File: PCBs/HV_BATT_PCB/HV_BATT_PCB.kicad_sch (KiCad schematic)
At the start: 66 parts, among them J47 Conn_01x02_Male, J48 Conn_01x10_Male, J49 Conn_01x08_Male, J50 Conn_01x02_Male, J51 Conn_01x02_Male, J52 Conn_01x02_Male, J53 Conn_01x02_Male, J54 Conn_01x14_Male, J55 Conn_01x06_Male, J56 Conn_01x04_Male, K10 LV_BATT_FAN, K7 PUMP, K8 FAN_R, K9 FAN_L, Q18 IRF640, Q19 IRF640, Q20 IRF640, U27 LR8, U28 LR8, U29 LR8, U30 LR8, U31 LR8, U32 LM311, U33 LR8, U34 4N35, U35 NE555P

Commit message: update schematics snapshot
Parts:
- removed C10: 1uF, Capacitor_THT:C_Disc_D4.3mm_W1.9mm_P5.00mm, symbol Device:C_Small
- removed C11: 1uF, Capacitor_THT:C_Axial_L3.8mm_D2.6mm_P15.00mm_Horizontal, symbol Device:C
- removed C12: 1uF, Capacitor_THT:CP_Radial_D8.0mm_P5.00mm, symbol Device:C_Polarized
- removed C7, C8: 2.2uF, Capacitor_THT:CP_Radial_D8.0mm_P5.00mm, symbol Device:C
- removed C9: 1nF, Capacitor_THT:C_Disc_D4.3mm_W1.9mm_P5.00mm, symbol Device:C_Small
- removed D28, D29, D31, D32, D33, D34: 1N5349, Diode_THT:D_DO-15_P10.16mm_Horizontal, symbol Diode:1N53xxB
- removed D30: TVS, Diode_SMD:D_SMC, symbol Diode:1.5KExxA
- removed F4: 3A Fuse, footprint:Fuse_Holder(GF-205B), symbol Device:Fuse
- removed J47: Conn_01x02_Male, Connector_AMASS:AMASS_XT30U-F_1x02_P5.0mm_Vertical, symbol Connector:Conn_01x02_Male
- removed J48: Conn_01x10_Male, Connector_Molex:Molex_Micro-Fit_3.0_43650-1015_1x10_P3.00mm_Vertical, symbol Connector:Conn_01x10_Male
- removed J49: Conn_01x08_Male, Connector_PinHeader_2.54mm:PinHeader_1x08_P2.54mm_Vertical, symbol Connector:Conn_01x08_Male
- removed J50: Conn_01x02_Male, Connector_PinHeader_2.54mm:PinHeader_2x01_P2.54mm_Vertical, symbol 11:Conn_01x02_Male
- removed J51, J52: Conn_01x02_Male, Connector_Molex:Molex_Micro-Fit_3.0_43650-0215_1x02_P3.00mm_Vertical, symbol Connector:Conn_01x02_Male
- removed J53: Conn_01x02_Male, Connector_PinHeader_2.54mm:PinHeader_2x01_P2.54mm_Vertical, symbol Connector:Conn_01x02_Male
- removed J54: Conn_01x14_Male, Connector_PinHeader_2.54mm:PinHeader_1x14_P2.54mm_Vertical, symbol Connector:Conn_01x14_Male
- removed J55: Conn_01x06_Male, Connector_PinHeader_2.54mm:PinHeader_1x06_P2.54mm_Vertical, symbol Connector:Conn_01x06_Male
- removed J56: Conn_01x04_Male, Connector_PinHeader_2.54mm:PinHeader_1x04_P2.54mm_Vertical, symbol Connector:Conn_01x04_Male
- removed K10: LV_BATT_FAN, Goolgle_Drive_Library:HR702, symbol Relay:DIPxx-1Cxx-51x
- removed K7: PUMP, Goolgle_Drive_Library:HR702, symbol Relay:DIPxx-1Cxx-51x
- removed K8: FAN_R, Goolgle_Drive_Library:HR702, symbol Relay:DIPxx-1Cxx-51x
- removed K9: FAN_L, Goolgle_Drive_Library:HR702, symbol Relay:DIPxx-1Cxx-51x
- removed Q18, Q19, Q20: IRF640, Goolgle_Drive_Library:IRF640NPBF, symbol Device:Q_NMOS_GDS
- removed R57, R58, R59, R60, R62, R63, R65, R67: 4.7M, Resistor_THT:R_Axial_DIN0207_L6.3mm_D2.5mm_P10.16mm_Horizontal, symbol Device:R_US
- removed R61: 1M, Resistor_THT:R_Axial_DIN0207_L6.3mm_D2.5mm_P10.16mm_Horizontal, symbol Device:R_US
- removed R64: 390k, Resistor_THT:R_Axial_DIN0207_L6.3mm_D2.5mm_P10.16mm_Horizontal, symbol Device:R_US
- removed R66: 4.7k, Resistor_THT:R_Axial_DIN0207_L6.3mm_D2.5mm_P10.16mm_Horizontal, symbol Device:R_US
- removed R68: 18k, Resistor_THT:R_Axial_DIN0207_L6.3mm_D2.5mm_P10.16mm_Horizontal, symbol Device:R_US
- removed R69: 12k, Resistor_THT:R_Axial_DIN0207_L6.3mm_D2.5mm_P10.16mm_Horizontal, symbol Device:R_US
- removed R70, R74: 10k, Resistor_THT:R_Axial_DIN0207_L6.3mm_D2.5mm_P10.16mm_Horizontal, symbol Device:R_US
- removed R71, R75: 2k2, Resistor_THT:R_Axial_DIN0207_L6.3mm_D2.5mm_P10.16mm_Horizontal, symbol Device:R_US
- removed R72: 1k, Resistor_THT:R_Axial_DIN0207_L6.3mm_D2.5mm_P10.16mm_Horizontal, symbol Device:R_US
- removed R73: 100k, Resistor_THT:R_Axial_DIN0207_L6.3mm_D2.5mm_P10.16mm_Horizontal, symbol Device:R_US
- removed R76, R77: 240k, Resistor_THT:R_Axial_DIN0207_L6.3mm_D2.5mm_P10.16mm_Horizontal, symbol Device:R_US
- removed U27, U28, U29, U30, U31, U33: LR8, Goolgle_Drive_Library:LR8N3-G, symbol Regulator_Linear:LR8K4-G
- removed U32: LM311, Goolgle_Drive_Library:LM311P, symbol Comparator:LM311
- removed U34: 4N35, Goolgle_Drive_Library:4N35, symbol Isolator:4N35
- removed U35: NE555P, Goolgle_Drive_Library:NE555P, symbol Timer:NE555P
- added BMS1: Conn_01x08_Male, Connector_PinHeader_2.54mm:PinHeader_1x08_P2.54mm_Vertical, symbol Connector:Conn_01x08_Male
- added C1, C2: 2.2uF, Capacitor_THT:CP_Radial_D8.0mm_P5.00mm, symbol Device:C
- added C3: 1nF, Capacitor_THT:C_Disc_D4.3mm_W1.9mm_P5.00mm, symbol Device:C_Small
- added C4: 1uF, Capacitor_THT:C_Disc_D4.3mm_W1.9mm_P5.00mm, symbol Device:C_Small
- added C5: 1uF, Capacitor_THT:C_Axial_L3.8mm_D2.6mm_P15.00mm_Horizontal, symbol Device:C
- added C6: 1uF, Capacitor_THT:CP_Radial_D8.0mm_P5.00mm, symbol Device:C_Polarized
- added D1, D2, D4, D5, D6, D7: 1N5349, Diode_THT:D_DO-15_P10.16mm_Horizontal, symbol Diode:1N53xxB
- added D3: TVS, Diode_SMD:D_SMC, symbol Diode:1.5KExxA
- added F1: SMCJ440A, Fuse:Fuseholder_Cylinder-5x20mm_Schurter_0031_8201_Horizontal_Open, symbol Device:Fuse
- added FAN,GND_{AIR1: Conn_01x04_Male, Connector_PinHeader_2.54mm:PinHeader_1x04_P2.54mm_Vertical, symbol Connector:Conn_01x04_Male
- added HV_{PCB1, J1, PRECHARGE2: Conn_01x02_Male, Connector_Molex:Molex_Micro-Fit_3.0_43650-0215_1x02_P3.00mm_Vertical, symbol Connector:Conn_01x02_Male
- added IMD1: Conn_01x06_Male, Connector_PinHeader_2.54mm:PinHeader_1x06_P2.54mm_Vertical, symbol Connector:Conn_01x06_Male
- added K1: PUMP, Goolgle_Drive_Library:HR702, symbol Relay:DIPxx-1Cxx-51x
- added K2: FAN_R, Goolgle_Drive_Library:HR702, symbol Relay:DIPxx-1Cxx-51x
- added K3: FAN_L, Goolgle_Drive_Library:HR702, symbol Relay:DIPxx-1Cxx-51x
- added K4: LV_BATT_FAN, Goolgle_Drive_Library:HR702, symbol Relay:DIPxx-1Cxx-51x
- added Q1, Q2, Q3: IRF640, Goolgle_Drive_Library:IRF640NPBF, symbol Device:Q_NMOS_GDS
- added R1, R11, R2, R3, R4, R6, R7, R9: 4.7M, Resistor_THT:R_Axial_DIN0207_L6.3mm_D2.5mm_P10.16mm_Horizontal, symbol Device:R_US
- added R10: 4.7k, Resistor_THT:R_Axial_DIN0207_L6.3mm_D2.5mm_P10.16mm_Horizontal, symbol Device:R_US
- added R12: 18k, Resistor_THT:R_Axial_DIN0207_L6.3mm_D2.5mm_P10.16mm_Horizontal, symbol Device:R_US
- added R13: 12k, Resistor_THT:R_Axial_DIN0207_L6.3mm_D2.5mm_P10.16mm_Horizontal, symbol Device:R_US
- added R14, R18: 10k, Resistor_THT:R_Axial_DIN0207_L6.3mm_D2.5mm_P10.16mm_Horizontal, symbol Device:R_US
- added R15, R19: 2k2, Resistor_THT:R_Axial_DIN0207_L6.3mm_D2.5mm_P10.16mm_Horizontal, symbol Device:R_US
- added R16: 1k, Resistor_THT:R_Axial_DIN0207_L6.3mm_D2.5mm_P10.16mm_Horizontal, symbol Device:R_US
- added R17: 100k, Resistor_THT:R_Axial_DIN0207_L6.3mm_D2.5mm_P10.16mm_Horizontal, symbol Device:R_US
- added R20, R21: 240k, Resistor_THT:R_Axial_DIN0207_L6.3mm_D2.5mm_P10.16mm_Horizontal, symbol Device:R_US
- added R5: 1M, Resistor_THT:R_Axial_DIN0207_L6.3mm_D2.5mm_P10.16mm_Horizontal, symbol Device:R_US
- added R8: 390k, Resistor_THT:R_Axial_DIN0207_L6.3mm_D2.5mm_P10.16mm_Horizontal, symbol Device:R_US
- added TEMP1: Conn_01x02_Male, Connector_PinHeader_2.54mm:PinHeader_2x01_P2.54mm_Vertical, symbol 11:Conn_01x02_Male
- added U1, U2, U3, U4, U5, U7: LR8, Goolgle_Drive_Library:LR8N3-G, symbol Regulator_Linear:LR8K4-G
- added U6: LM311, Goolgle_Drive_Library:LM311P, symbol Comparator:LM311
- added U8: 4N35, Goolgle_Drive_Library:4N35, symbol Isolator:4N35
- added U9: NE555P, Goolgle_Drive_Library:NE555P, symbol Timer:NE555P
- added VI1: Conn_01x02_Male, Connector_PinHeader_2.54mm:PinHeader_2x01_P2.54mm_Vertical, symbol Connector:Conn_01x02_Male
- added asdf1: Conn_01x10_Male, Connector_Molex:Molex_Micro-Fit_3.0_43650-1015_1x10_P3.00mm_Vertical, symbol Connector:Conn_01x10_Male
- added dff1: Conn_01x14_Male, Connector_PinHeader_2.54mm:PinHeader_1x14_P2.54mm_Vertical, symbol Connector:Conn_01x14_Male
- F2: value SMCJ440A -> 1A Fuse; footprint Goolgle_Drive_Library:Fuse_Holder(GF-205B) -> Fuse:Fuseholder_Cylinder-5x20mm_Schurter_0031_8201_Horizontal_Open
- F3: value 1A Fuse -> 3A Fuse; footprint footprint:Fuse_Holder(GF-205B) -> Fuse:Fuseholder_Cylinder-5x20mm_Schurter_0031_8201_Horizontal_Open
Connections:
- net GND is gone; now on net GND_AIR: PRECHARGE1.5 (COIL_2)
- net BMS_FAULT: now also BMS1.2 (Pin_2), dff1.4 (Pin_4)
- net CAN_H_{BMS: now also BMS1.4 (Pin_4), dff1.8 (Pin_8)
- net CAN_L_{BMS: now also BMS1.5 (Pin_5), dff1.9 (Pin_9)
- net CHARGER_SAFETY: now also BMS1.7 (Pin_7), dff1.12 (Pin_12)
- net CHARGE_POWER: now also BMS1.6 (Pin_6), dff1.11 (Pin_11)
- net GND_AIR: now also BMS1.3 (Pin_3), FAN,GND_{AIR1.3 (Pin_3), IMD1.1 (Pin_1), IMD1.3 (Pin_3), IMD1.4 (Pin_4), Q1.3 (S), Q2.3 (S), Q3.3 (S), R17.1, R19.2, TEMP1.2 (Pin_2), dff1.2 (Pin_2)
- net HV_{PCB}+: now also D1.1 (K), HV_{PCB1.1 (Pin_1), R1.1
- net HV_{PCB}-: now also C1.2, C2.2, C5.2, D7.2 (A), HV_{PCB1.2 (Pin_2), R11.2, R12.2, R16.2, R5.2, R8.2, U6.1 (GND), U6.4 (V-), U8.2
- net IMD_FAULT: now also IMD1.5 (Pin_5), R19.1, dff1.3 (Pin_3)
- net LV_{BATT_FAN}+: now also FAN,GND_{AIR1.1 (Pin_1), K2.14
- net LV_{BATT_FAN}-: now also FAN,GND_{AIR1.2 (Pin_2), asdf1.7 (Pin_7), asdf1.8 (Pin_8), asdf1.9 (Pin_9)
- net LV_{BMS}+: now also F2.2, BMS1.1 (Pin_1); no longer F3.2
- net LV_{COOLING1}: now also K1.7, K1.8, K2.7, K2.8, K3.7, K3.8, K4.7, K4.8
- net LV_{FAN_L}+: now also K3.14, asdf1.5 (Pin_5)
- net LV_{FAN_R}+: now also K4.14, asdf1.4 (Pin_4)
- net LV_{IMD}+: now also F3.2, IMD1.2 (Pin_2)
- net LV_{PACK}+: now also F2.1, K1.2, K2.2, K3.2, K4.2, R18.1, R20.2, TEMP1.1 (Pin_1), U8.5, U9.4 (R), U9.8 (VCC), asdf1.3 (Pin_3), dff1.1 (Pin_1)
- net LV_{PUMP}+: now also K1.14, asdf1.6 (Pin_6)
- net ON_{BATT_FAN}: now also K2.6, dff1.7 (Pin_7)
- net ON_{COOLING: now also dff1.13 (Pin_13)
- net ON_{PUMP}: now also K1.6, dff1.5 (Pin_5)
- net ON_{RAD_FAN}: now also K3.6, K4.6, dff1.6 (Pin_6)
- net PRECHARGE_DRIVE: now also dff1.10 (Pin_10)
- net RELAY_PRECHARGE: now also PRECHARGE2.1 (Pin_1)
- net R_PRECHARGE: now also PRECHARGE2.2 (Pin_2)
- net TSAL_GREEN: now also Q1.2 (D), asdf1.1 (Pin_1)
- net TSAL_RED: now also U9.3 (Q), asdf1.2 (Pin_2)
- net VI_LED+: now also C5.1, R13.1, U4.2 (OUT), U5.2 (OUT), U7.2 (OUT), VI1.1 (Pin_1)
- net VI_LED-: now also R16.1, VI1.2 (Pin_2)
- net at PS2.1 (+VIN): now also D3.1 (A1), F1.2; no longer F2.2
- net at PS2.3 (-VIN): now also D3.2 (A2), J1.1 (Pin_1)
- net at PS1.6 (+VOUT): now also C4.1, R14.1, R6.1, U6.8 (V+)
- new net: R14.2, R15.1, U6.7
- new net: R15.2, U8.1
- new net: R6.2, R7.1
- new net: C6.2, Q3.2 (D), U9.1 (GND)
- new net: C6.1, R21.1, U9.2 (TR), U9.6 (THR)
- new net: R20.1, R21.2, U9.7 (DIS)
- new net: C1.1, D6.2 (A), U1.1 (IN), U2.1 (IN), U3.1 (IN)
- new net: C2.1, R10.1, U1.2 (OUT), U2.2 (OUT), U3.2 (OUT), U4.1 (IN), U5.1 (IN), U7.1 (IN)
- new net: R10.2, R8.1, U1.3 (ADJ), U2.3 (ADJ), U3.3 (ADJ)
- new net: D5.2 (A), D6.1 (K)
- new net: R2.2, R3.1
- new net: R3.2, R4.1
- new net: F1.1, J1.2 (Pin_2)
- new net: Q2.1 (G), Q3.1 (G), R17.2, U8.4
- new net: C3.1, R11.1, R9.2, U6.3 (-)
- new net: D2.2 (A), D4.1 (K)
- new net: D4.2 (A), D5.1 (K)
- new net: R12.1, R13.2, U4.3 (ADJ), U5.3 (ADJ), U7.3 (ADJ)
- new net: D1.2 (A), D2.1 (K)
- new net: Q1.1 (G), Q2.2 (D), R18.2
- new net: C3.2, D7.1 (K), R4.2, R5.1, U6.2 (+)
- new net: R1.2, R2.1
- new net: C4.2, U6.5 (BAL), U6.6 (STRB)
- new net: R7.2, R9.1
- no-connect marks 17 -> 22
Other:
- note added: "LV, HV distance..."

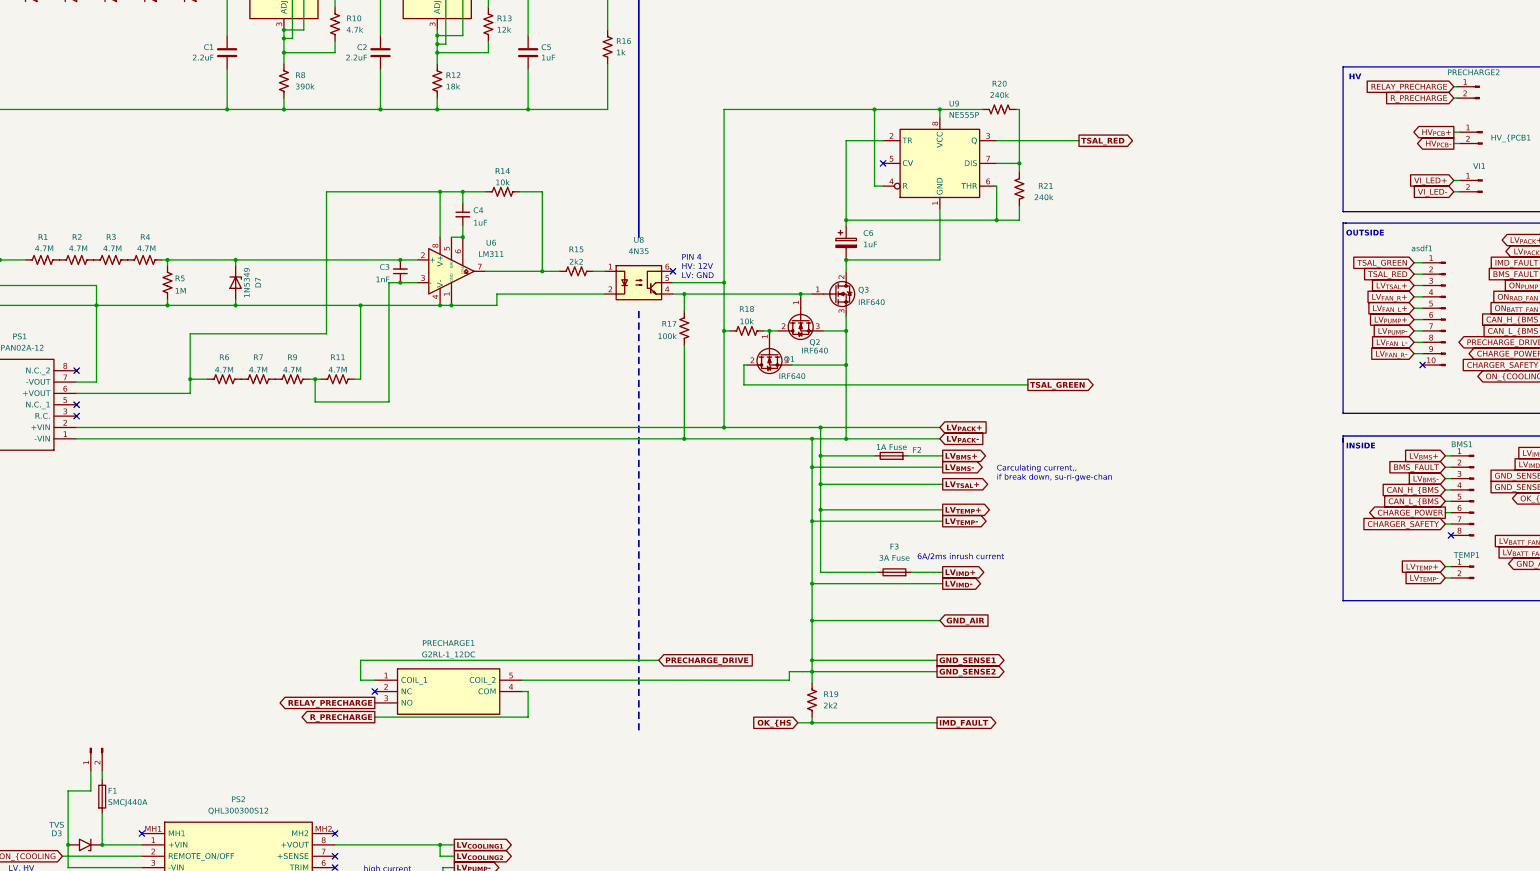
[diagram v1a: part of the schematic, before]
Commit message: update: schematics and wirings to current state
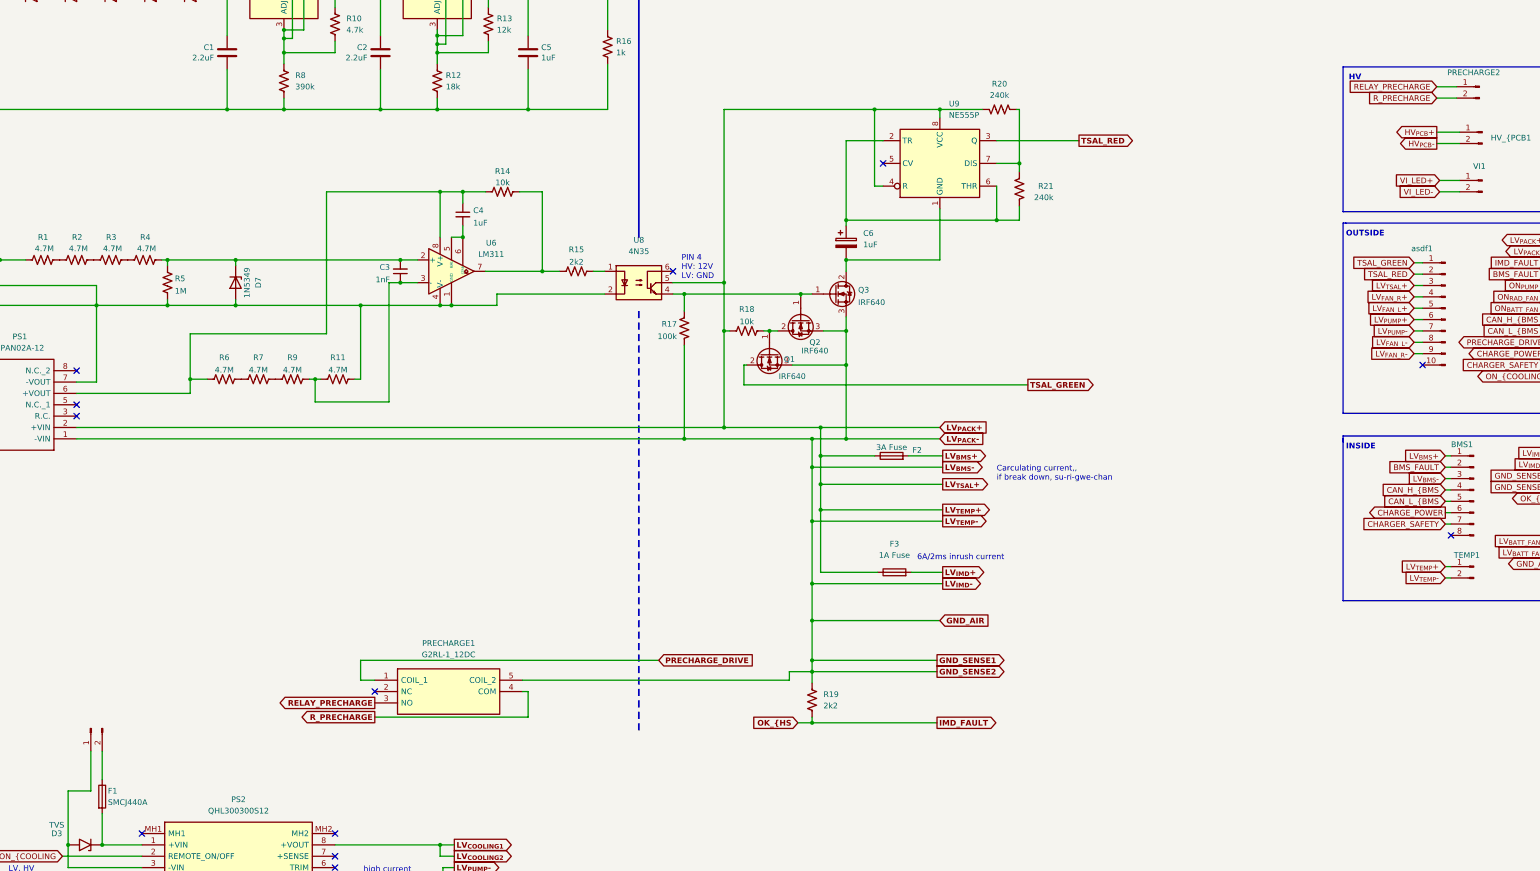
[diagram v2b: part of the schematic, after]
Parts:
- F2: value 1A Fuse -> 3A Fuse
- F3: value 3A Fuse -> 1A Fuse
